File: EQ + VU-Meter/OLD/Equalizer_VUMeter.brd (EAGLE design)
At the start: 116 x 38.7 mm, 220 parts, among them IC1 TL074D, IC2 TL074D, IC3 TL074D, IC4 TL074D, T1 BC846A, T10 BC846A, T11 BC846A, T12 BC846A, T13 BC846A, T14 BC846A, T15 BC846A, T16 BC846A, T17 BC846A, T18 BC846A, T19 BC846A, T2 BC846A, T20 BC846A, T21 BC846A, T22 BC846A, T23 BC846A, T24 BC846A, T25 BC846A, T26 BC846A, T27 BC846A, T28 BC846A, T29 BC846A, T3 BC846A, T30 BC846A, T4 BC846A, T5 BC846A, T6 BC846A, T7 BC846A, T8 BC846A, T9 BC846A

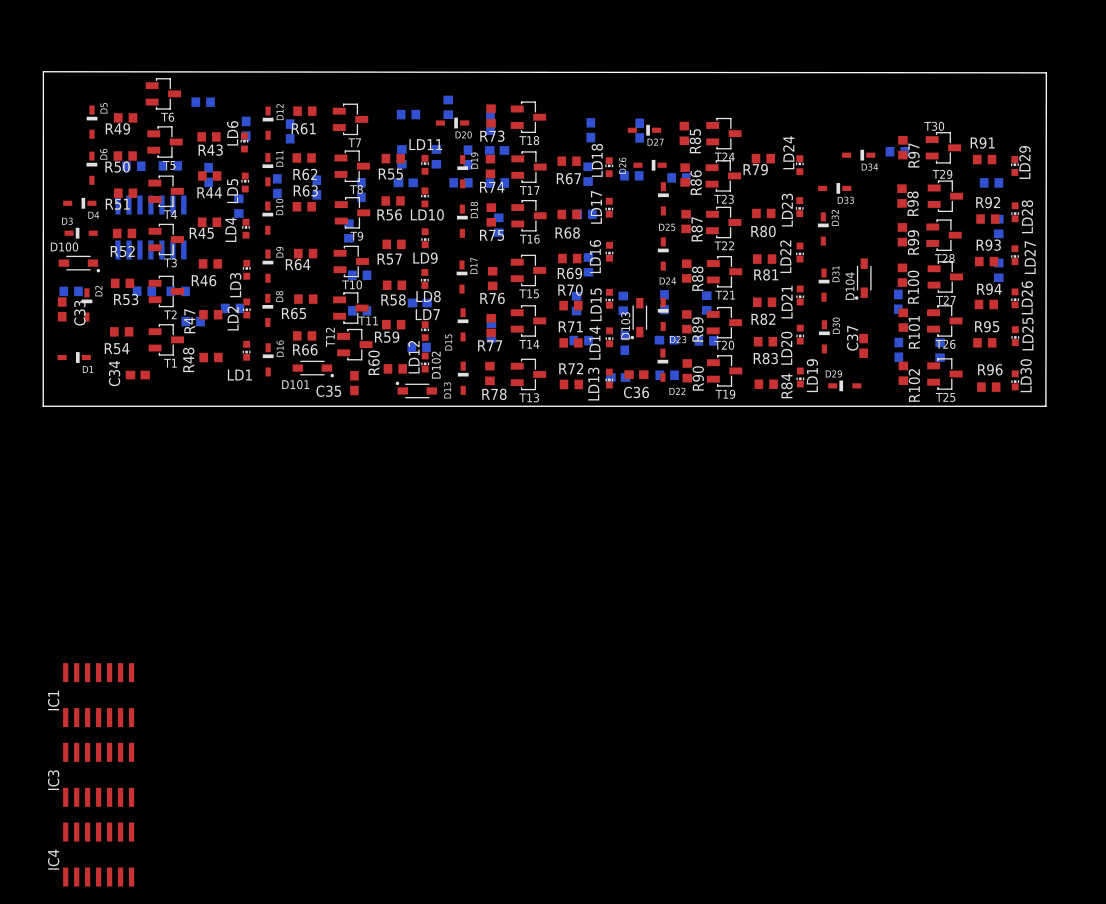
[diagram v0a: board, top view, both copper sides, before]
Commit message: Production data for ordering Mainboard, Keys, UI and EQ at JLCPCB
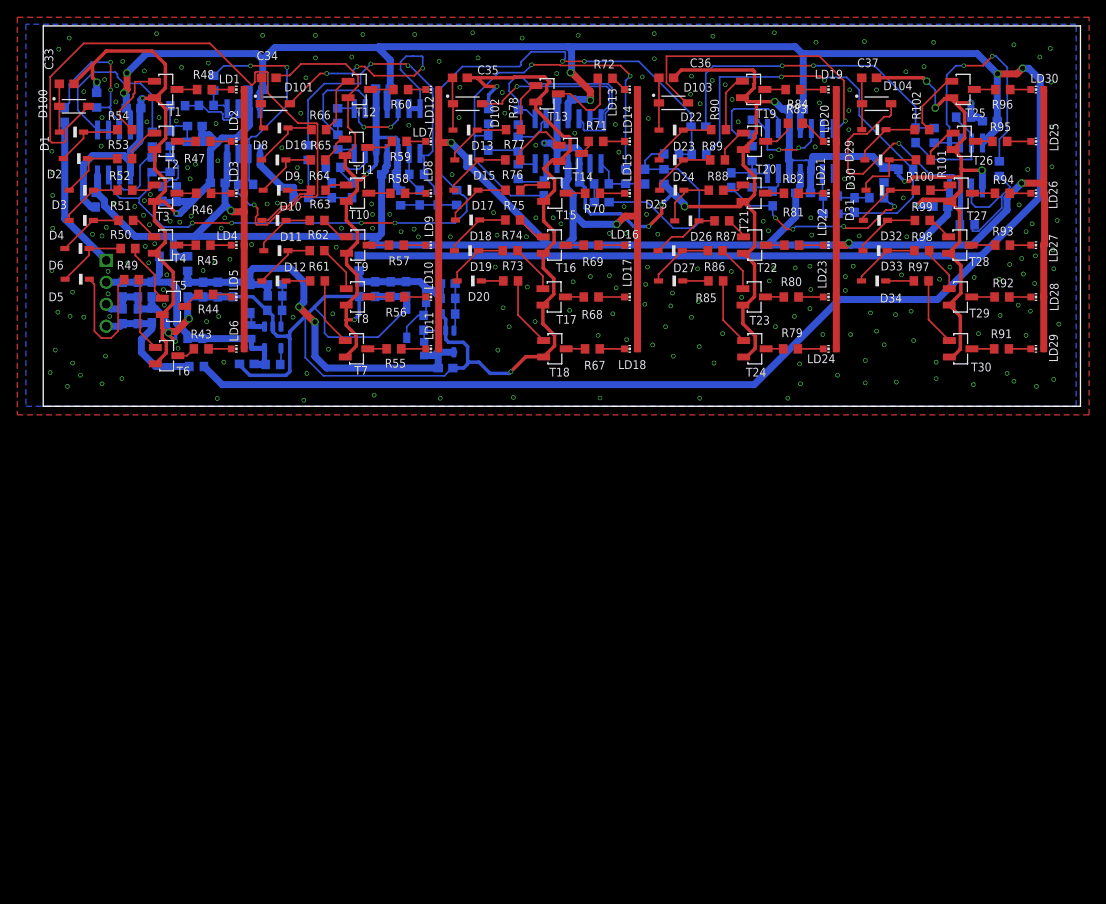
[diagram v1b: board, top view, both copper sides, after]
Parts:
- added C10, C11, C12, C13, C27, C28, C29, C32, C39, C4, C8, C9: 100n, rcl:C0603
- added C14, C40, C41, C42, C43, C44, C45, C46, C47, C48, C49, C50: 10u, rcl:C0603
- added C5: 2.2 uF, rcl:C0603
- added C7: 4.7 uF, rcl:C0603
- added CCUK: 1 uF, rcl:C0603
- added CF: 220 pF, rcl:C0603
- added CFF: 330 pF, rcl:C0603
- added CIN, COUT: 22 uF, rcl:C0603
- added D14, D7: (no value), MMSZ5226B-7-F:SOD3715X135L32X57N
- added IC5, IC7: TL072D, linear:SO08
- added J2: 640455-4, 640455-4:TE_640455-4
- added L1, L2, L3: 10 uH, ASMCI-0603-100M-T:INDC1608X95N
- added R103, R104, R105: 0, rcl:R0603
- added R31: 68 K, rcl:R0603
- added R32: 51K, rcl:R0603
- added R35: 13.3K, rcl:R0603
- added R41: 3.3k, rcl:R0603
- added R42: 35K, rcl:R0603
- added RFB1: 29.4K, rcl:R0603
- added RFB2: 5.76K, rcl:R0603
- added U1: LM2611, LM2611BMFX_NOPB:SOT95P280X145-5N
- added U2: LMR62014, LMR62014XMF_NOPB:SOT95P280X145-5N
- IC1: value TL074D -> TL072D; device linear:SO14 -> linear:SO08
- R26: value 3.3k -> 0
- R27: value 35K -> 0
- moved IC4 115.0 mm to (87.6, 29.5), flipped to the bottom
- moved IC3 91.2 mm to (60.7, 30.7), flipped to the bottom
- moved R27 83.1 mm to (16.7, 16.5), turned to 90 degrees
- moved IC1 67.4 mm to (23.2, 31.8), flipped to the bottom, turned to 180 degrees
- moved R26 46.3 mm to (17.6, 7.85), turned to 180 degrees
- moved R34 41.1 mm to (99.8, 27.4), turned to 180 degrees
- moved C34 37.6 mm to (26.1, 38.0)
- moved C35 37.4 mm to (48.2, 38.0), turned to 0 degrees
- moved R72 35.6 mm to (65.0, 37.9)
- moved C36 34.5 mm to (72.1, 38.0), turned to 0 degrees
- moved R96 34.5 mm to (111.0, 36.6)
- moved R84 34.2 mm to (86.7, 36.6)
- moved R37 34.1 mm to (97.3, 26.7), turned to 270 degrees
- moved LD30 33.7 mm to (115.0, 36.6), turned to 90 degrees
- moved D102 33.7 mm to (49.1, 35.0)
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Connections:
- removed net +8V: IC1.4, IC2.4, IC3.4, IC4.4, LD1.A, LD10.A, LD11.A, LD12.A, LD13.A, LD14.A, LD15.A, LD16.A, LD17.A, LD18.A, LD19.A, LD2.A, LD20.A, LD21.A, LD22.A, LD23.A, LD24.A, LD25.A, LD26.A, LD27.A, LD28.A, LD29.A, LD3.A, LD30.A, LD4.A, LD5.A, LD6.A, LD7.A, LD8.A, LD9.A
- removed net -8V: IC1.11, IC2.11, IC3.11, IC4.11
- removed net 3.3V: C38.2
- removed net N$1: C2.1, C3.1
- removed net N$14: IC3.13, R26.2, R27.1
- removed net N$6: C1.1, C6.1
- removed net TP_OUT1: IC2.8, R6.2
- removed net TP_OUT2: IC3.7, R25.2
- removed net TP_OUT3: IC3.14, R27.2
- new net +7,5V: C45.2, C46.1, C47.1, C7.1, CF.1, CIN.1, D7.1, L2.1, R27.1, R31.2, U1.4, U1.5
- new net -7,5V: C48.2, C49.1, C50.1, CFF.1, COUT.1, L3.2, R105.1, RFB1.1
- new net IN2,1V: C38.2, J2.1
- new net MAIN-5V: C14.2, C43.1, C44.1, J2.4, R103.1
- new net N$100: IC3.12, IC3.8, R25.2
- new net N$115: IC2.12, IC2.8, R6.2
- new net N$126: CCUK.2, D14.2, L3.1
- new net N$141: CCUK.1, L2.2, U1.1
- new net N$152: CFF.2, RFB1.2, RFB2.1, U1.3
- new net N$16: C17.1, R29.2
- new net N$18: C21.1, IC3.7, R18.2, R19.1
- new net N$181: IC2.7, R3.1
- new net N$183: IC4.9, R41.2, R42.1
- new net N$21: R32.1, U2.4
- new net N$22: CF.2, R31.1, R35.1, U2.3
- new net N$25: IC4.12, IC4.8, R42.2
- new net N$48: C25.1, IC4.7, R38.2, R41.1
- new net N$74: D7.2, L1.2, U2.1
- new net PB5V: C40.2, C41.1, C42.1, C5.1, J2.2, L1.1, R104.2, R26.1, R26.2, R32.2, U2.5
- new net V+: C27.1, C28.1, C29.1, C32.1, C39.1, C9.1, IC1.8, IC2.4, IC3.4, IC4.4, IC5.8, IC7.8, LD1.A, LD10.A, LD11.A, LD12.A, LD13.A, LD14.A, LD15.A, LD16.A, LD17.A, LD18.A, LD19.A, LD2.A, LD20.A, LD21.A, LD22.A, LD23.A, LD24.A, LD25.A, LD26.A, LD27.A, LD28.A, LD29.A, LD3.A, LD30.A, LD4.A, LD5.A, LD6.A, LD7.A, LD8.A, LD9.A, R104.1, R27.2
- new net V-: C10.2, C11.2, C12.2, C13.2, C4.2, C8.2, IC1.4, IC2.11, IC3.11, IC4.11, IC5.4, IC7.4, R103.2, R105.2
- net BP1_OUT: now also IC2.13, IC2.14; no longer C17.1, IC2.7, R29.2, R3.1
- net BP2_OUT: now also IC3.13, IC3.14; no longer C21.1, IC3.1, R18.2, R19.1
- net BP3_OUT: now also IC4.13, IC4.14; no longer C25.1, IC4.1, R26.1, R38.2
- net GND: now also C10.1, C11.1, C12.1, C13.1, C14.1, C27.2, C28.2, C29.2, C32.2, C39.2, C4.1, C40.1, C41.2, C42.2, C43.2, C44.2, C45.1, C46.2, C47.2, C48.1, C49.2, C5.2, C50.2, C7.2, C8.1, C9.2, CIN.2, COUT.2, D14.1, IC1.3, IC4.10, IC5.5, IC7.5, J2.3, R35.2, RFB2.2, U1.2, U2.2; no longer IC1.10, IC1.12, IC2.12, IC3.12
- net HP_OUT: now also IC7.7; no longer IC4.7
- net N$10: now also IC1.6; no longer IC1.13
- net N$19: now also IC3.2; no longer IC2.13
- net N$2: now also C1.1, C6.1
- net N$20: now also IC3.1; no longer IC2.14
- net N$24: now also IC3.6; no longer IC3.2
- net N$26: now also IC4.1; no longer IC3.8
- net N$28: now also IC4.2; no longer IC3.9
- net N$29: now also IC5.6; no longer IC1.6
- net N$3: now also IC1.2; no longer IC1.9
- net N$32: now also IC4.6; no longer IC4.2
- net N$34: now also IC7.3; no longer IC4.10
- net N$36: now also IC7.1, IC7.2; no longer IC4.8, IC4.9
- net N$39: now also IC7.6; no longer IC4.6
- net N$4: now also C2.1, C3.1
- net N$42: now also IC5.1, IC5.2; no longer IC1.1, IC1.2
- net N$47: now also IC5.3; no longer IC1.3
- net N$5: now also IC5.7; no longer IC1.7
- net N$8: now also IC1.1; no longer IC1.8
- net N$9: now also IC3.9; no longer IC3.6
- net TP_OUT: now also IC1.7; no longer IC1.14
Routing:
- net GND: track 0.00 -> 577.5 mm, vias 0 -> 22
- net V+: track 0.00 -> 355.1 mm, vias 0 -> 5
- net V-: track 0.00 -> 352.1 mm, vias 0 -> 6
- net N$5: track 0.00 -> 108.3 mm, vias 0 -> 6
- net TP_OUT: track 0.00 -> 80.5 mm, vias 0 -> 1
- net N$27: track 0.00 -> 51.3 mm, vias 0 -> 2
- net N$23: track 0.00 -> 51.1 mm, vias 0 -> 2
- net +7,5V: track 0.00 -> 50.3 mm, vias 0 -> 2
- net N$38: track 0.00 -> 37.4 mm, vias 0 -> 2
- net N$13: track 0.00 -> 37.0 mm, vias 0 -> 2
- net HP_OUT: track 0.00 -> 36.8 mm, vias 0 -> 1
- net BP3_OUT: track 0.00 -> 36.1 mm, vias 0 -> 1
- net PB5V: track 0.00 -> 31.4 mm
- net N$36: track 0.00 -> 30.8 mm, vias 0 -> 2
- net BP1_OUT: track 0.00 -> 29.9 mm, vias 0 -> 3
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- added copper zone on layer 1, net GND
- added copper zone on layer 16, net GND
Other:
- board size 116 x 38.7 mm -> 120 x 44 mm
- board text added: "Body - Synth Equalizer & VU Meter DSP - Lab SS21"
